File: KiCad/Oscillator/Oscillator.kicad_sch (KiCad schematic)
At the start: 37 parts, among them Q1 NPN, Q2 PNP, Q3 NPN, Q4 PNP, U4 40106, U5 TL074, U7 TL074

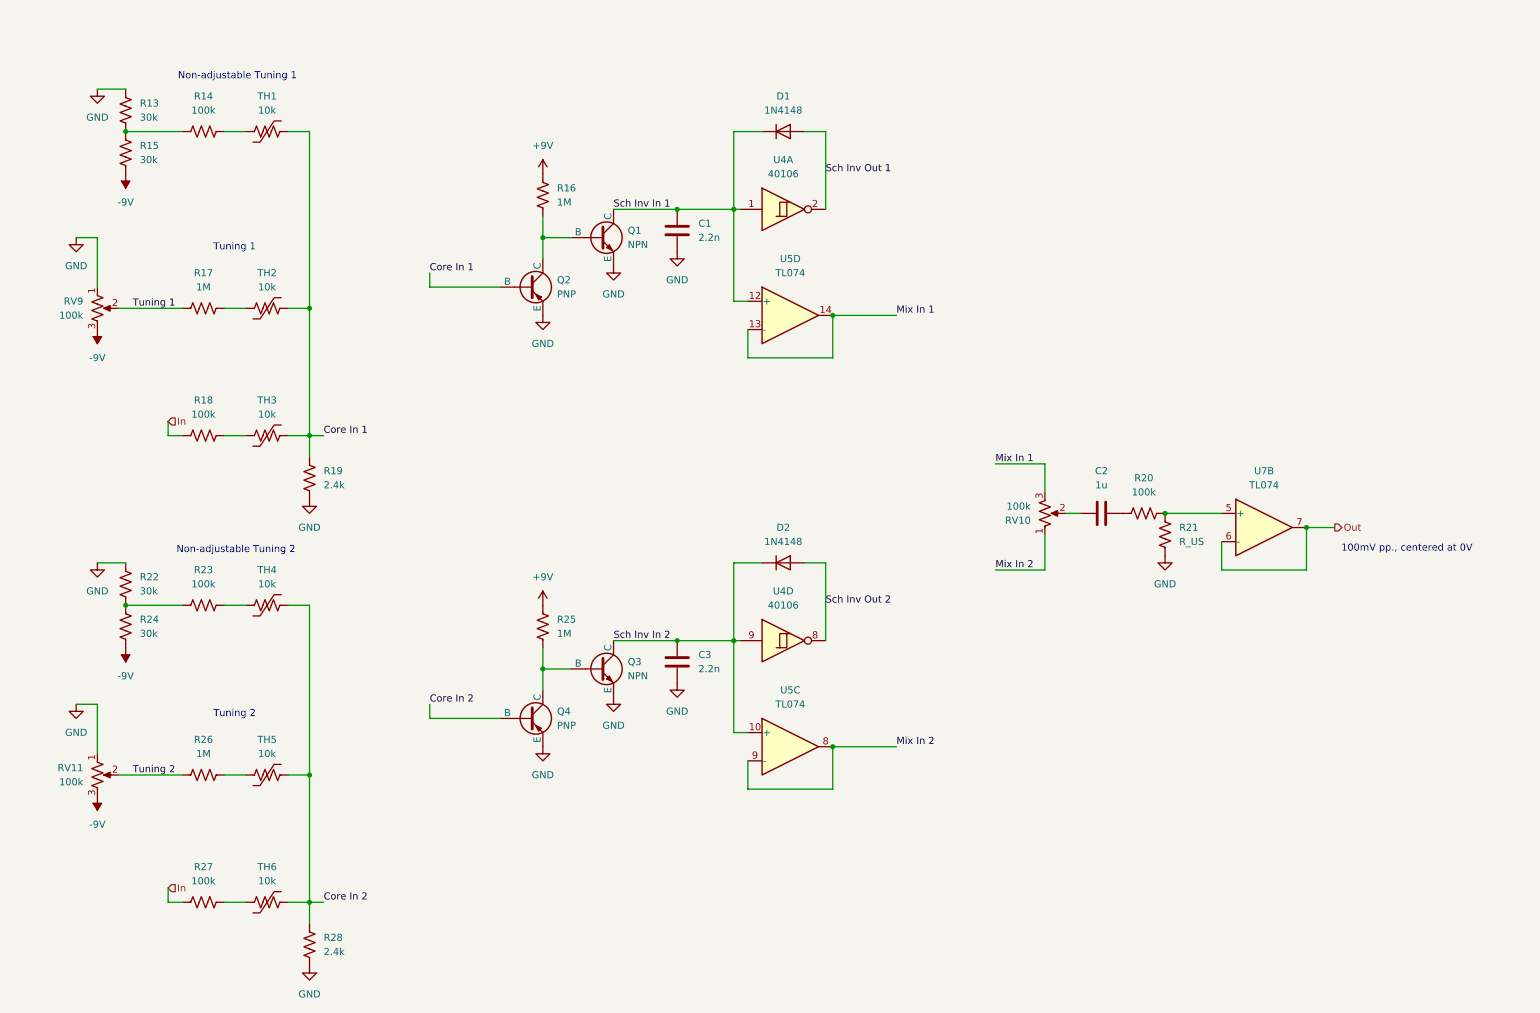
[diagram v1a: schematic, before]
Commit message: finished separating into separate kicad projects
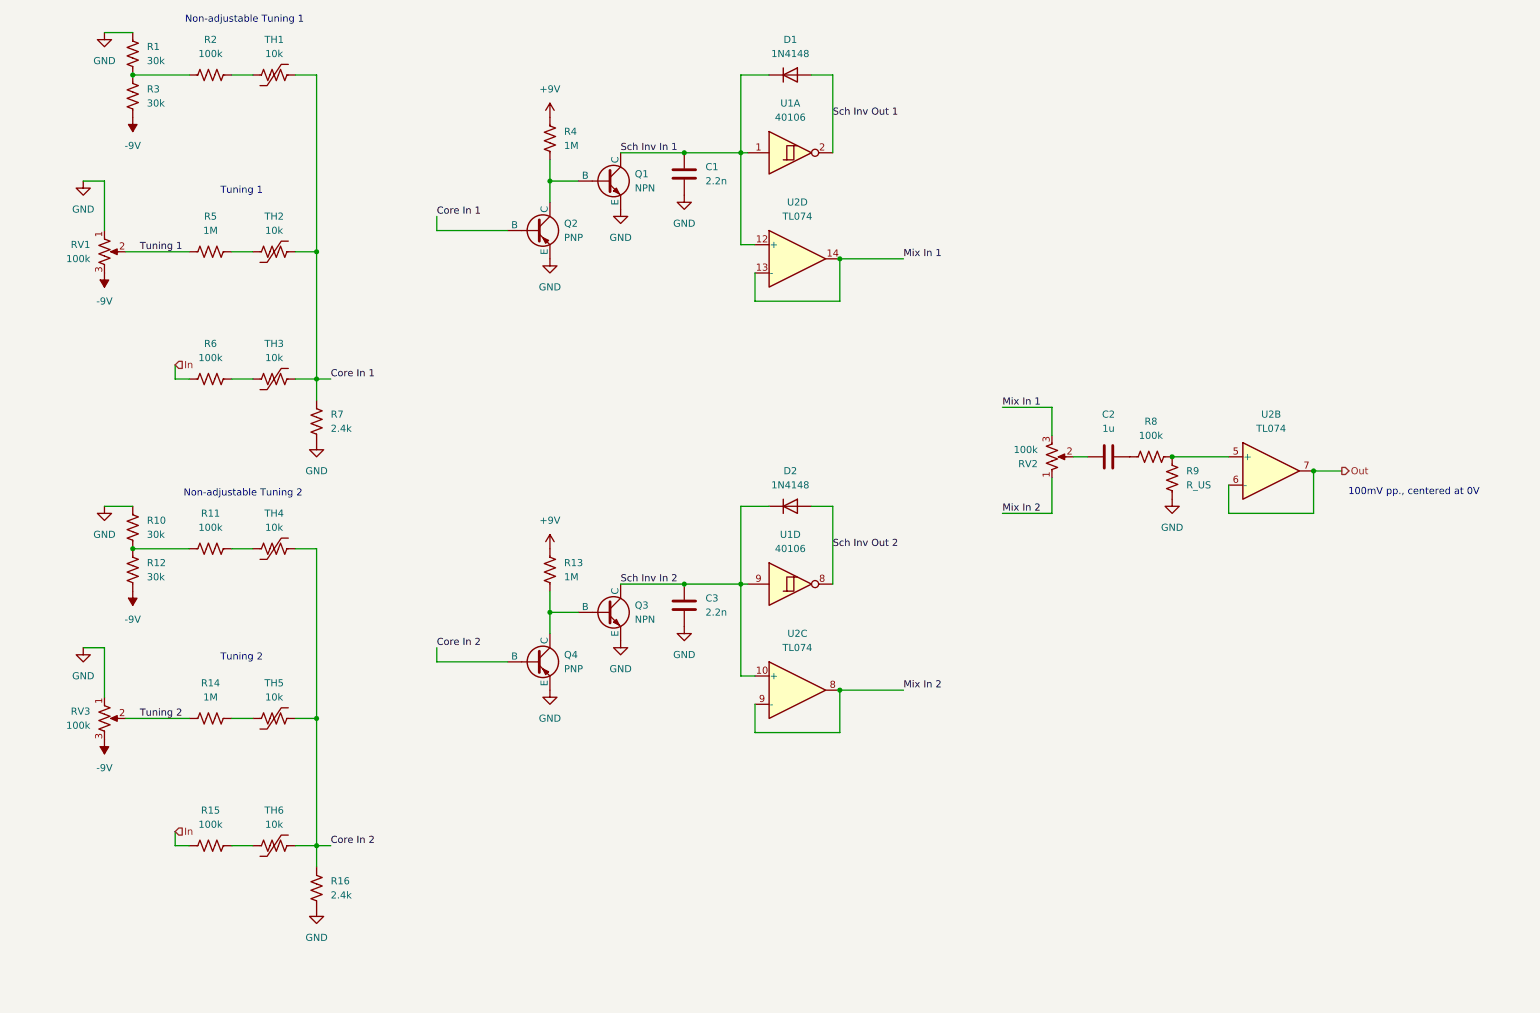
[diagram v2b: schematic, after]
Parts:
- removed RV9: 100k, Potentiometer 100k PTV09A-2020F-B104:Potentiometer 100k PTV09A-2020F-B104, symbol Device:R_Potentiometer_US
- removed U4: 40106, Schmitt Inv. CD40106BE:N14, symbol 4xxx:40106
- removed U5, U7: TL074, Package_DIP:DIP-14_W7.62mm, symbol Amplifier_Operational:TL074
- added RV1: 100k, Potentiometer 100k PTV09A-2020F-B104:Potentiometer 100k PTV09A-2020F-B104, symbol Device:R_Potentiometer_US
- added U1: 40106, Schmitt Inv. CD40106BE:N14, symbol 4xxx:40106
- added U2: TL074, Package_DIP:DIP-14_W7.62mm, symbol Amplifier_Operational:TL074
- renumbered R13 to R1, R22 to R10, R23 to R11, R24 to R12, R25 to R13, R26 to R14, R27 to R15, R28 to R16, R14 to R2, R15 to R3, R16 to R4, R17 to R5, R18 to R6, R19 to R7, R20 to R8, R21 to R9, RV10 to RV2, RV11 to RV3
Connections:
- net -9V: now also RV1.3
- net GND: now also RV1.1
- net Mix In 1: now also U2.13 (-), U2.14
- net Mix In 2: now also U2.8, U2.9 (-)
- net Out: now also U2.6 (-), U2.7
- net Sch Inv In 1: now also U1.1, U2.12 (+)
- net Sch Inv In 2: now also U1.9, U2.10 (+)
- net Sch Inv Out 1: now also U1.2
- net Sch Inv Out 2: now also U1.8
- net Tuning 1: now also RV1.2
- net at R8.2, R9.2: now also U2.5 (+)
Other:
- moved on the sheet: C1, C2, C3, D1, D2, Q1, Q2, Q3, Q4, R1, R10, R11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

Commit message: fixed critical issue in oscillator
schmitt trigger's VEE is supposed to be 0V, not -9V :wilted_rose: :wilted_rose:
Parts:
- removed R8: 100k, Resistor_SMD:R_0603_1608Metric, symbol Device:R_US
- removed R9: R_US, Resistor_THT:R_Axial_DIN0207_L6.3mm_D2.5mm_P7.62mm_Horizontal, symbol Device:R_US
- added J1: Screw_Terminal_01x02, symbol Connector:Screw_Terminal_01x02
- added RV3: 100k, symbol Device:R_Potentiometer_Trim_US
- added U3: TL074, Package_DIP:DIP-14_W7.62mm, symbol Amplifier_Operational:TL074
- renumbered R12 to R10, R13 to R11, R14 to R12, R15 to R13, R16 to R14, R10 to R8, R11 to R9, RV3 to RV4
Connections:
- net GND: now also RV3.3
- net In: now also J1.1 (Pin_1)
- net Out: now also J1.2 (Pin_2)
- net at U2.5 (+): now also RV3.2
- net at C2.2: now also RV3.1
- net at C2.1: now also U3.6 (-), U3.7; no longer RV2.2
- new net: RV2.2, U3.5 (+)
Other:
- moved on the sheet: C2, RV2, U2B

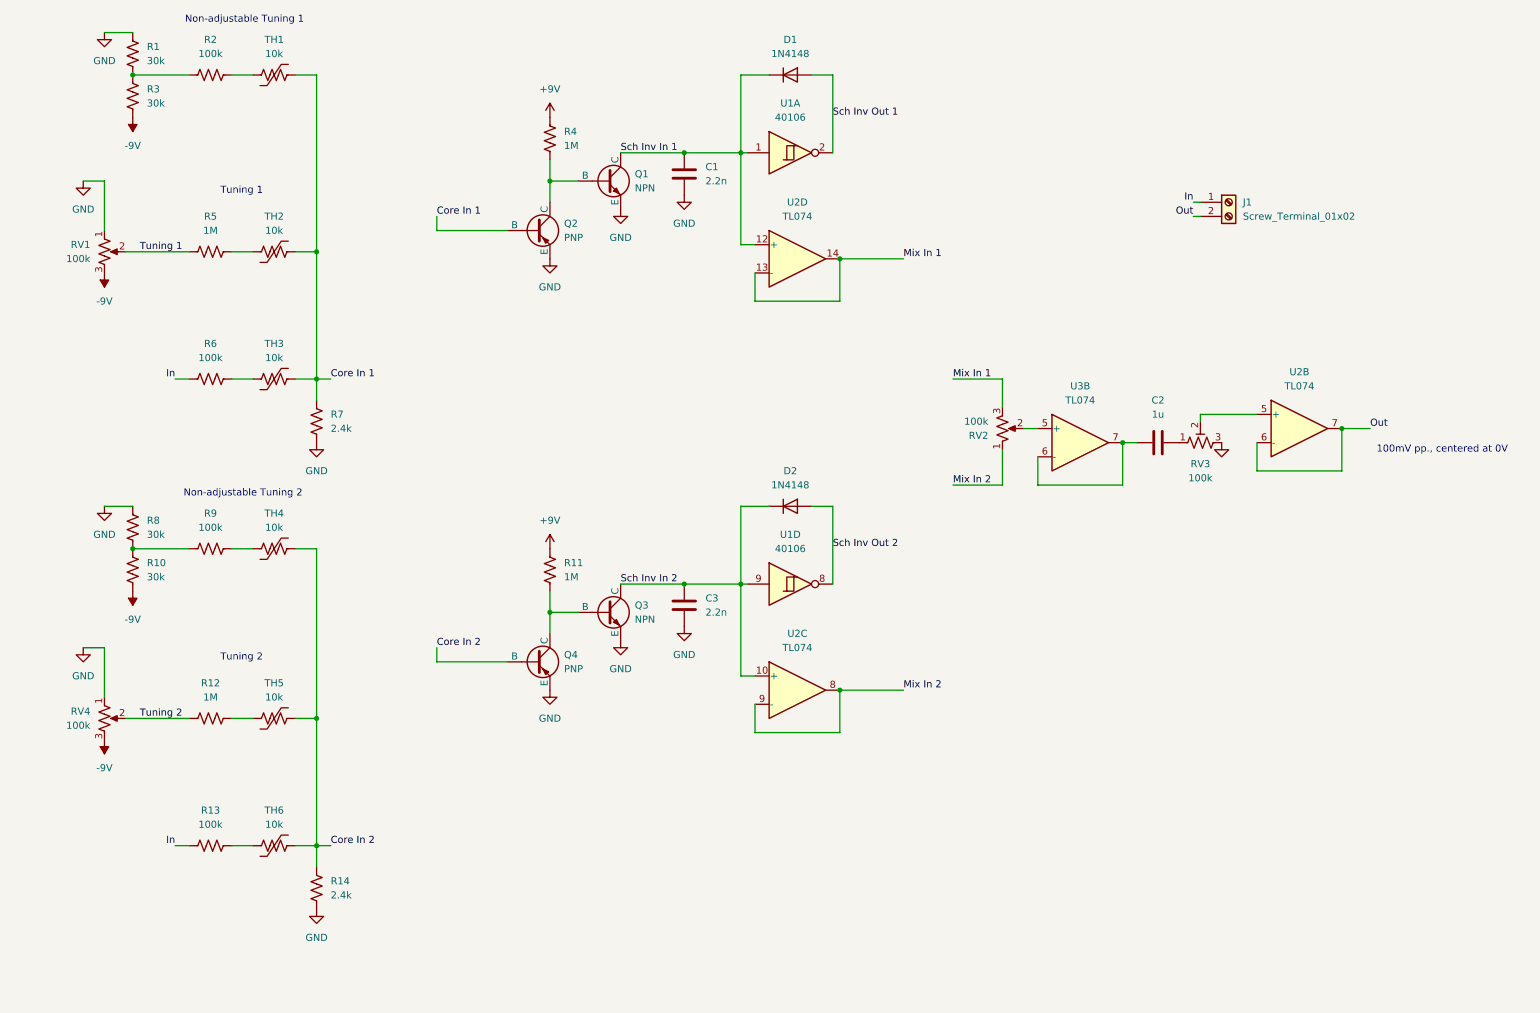
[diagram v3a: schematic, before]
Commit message: made oscillator more adjustable
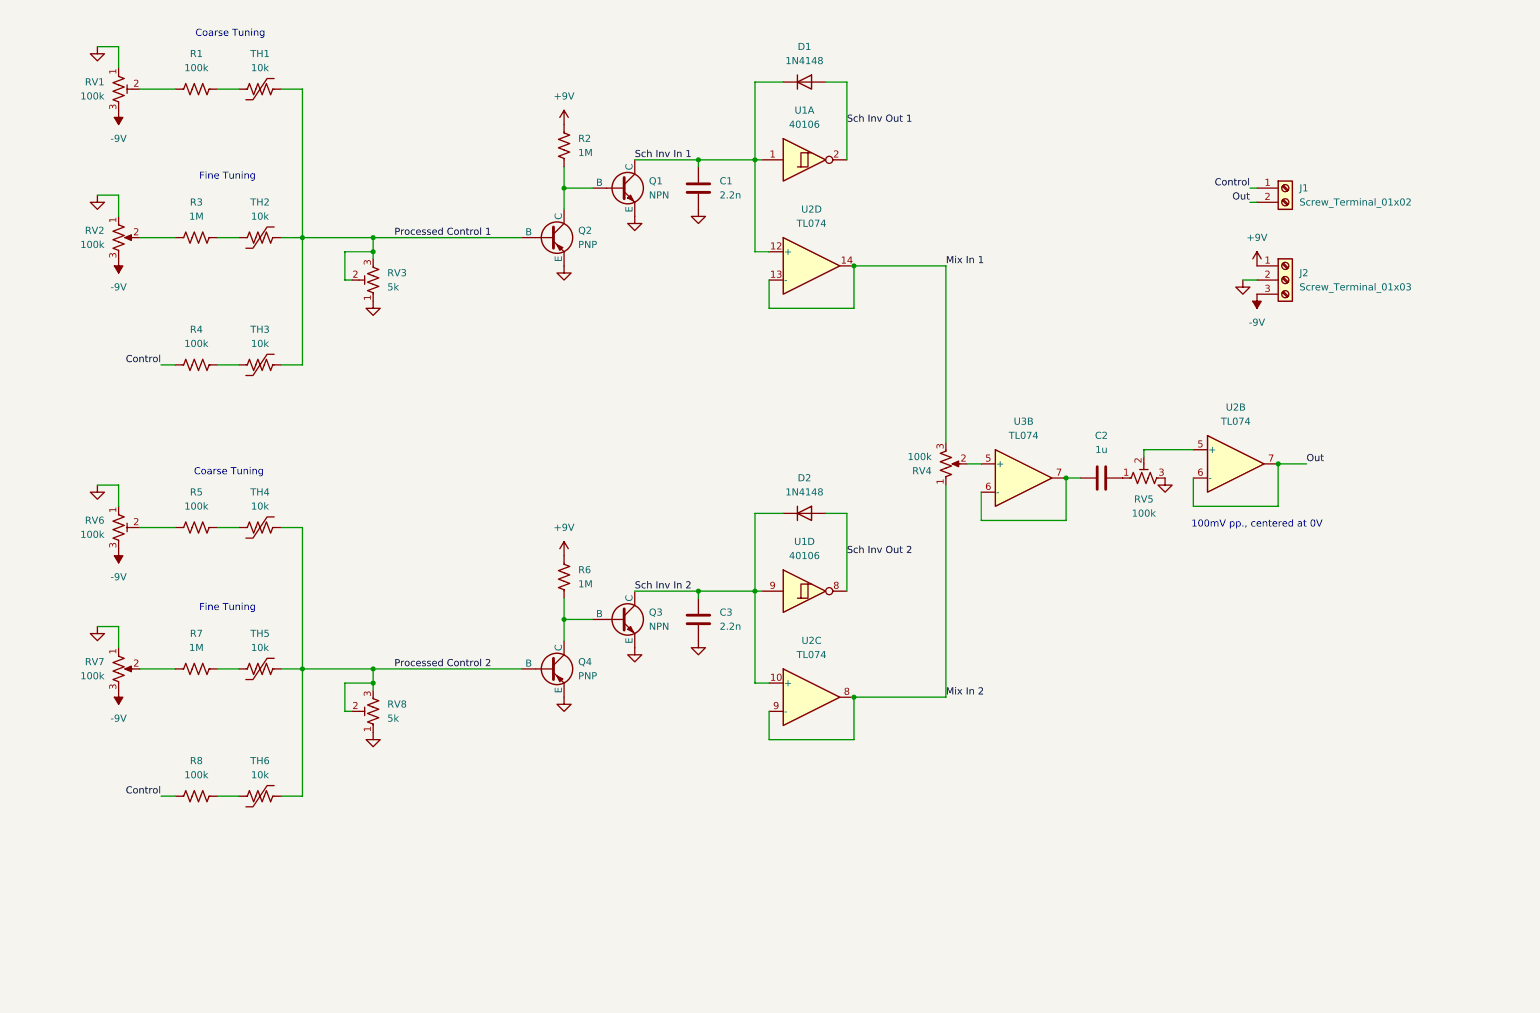
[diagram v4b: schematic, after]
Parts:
- removed R1, R10, R3, R8: 30k, Resistor_SMD:R_0603_1608Metric, symbol Device:R_US
- removed R14, R7: 2.4k, Resistor_SMD:R_0603_1608Metric, symbol Device:R_US
- added J2: Screw_Terminal_01x03, symbol Connector:Screw_Terminal_01x03
- added RV1, RV6: 100k, symbol Device:R_Potentiometer_Trim_US
- added RV3, RV8: 5k, symbol Device:R_Potentiometer_Trim_US
- renumbered R2 to R1, R4 to R2, R5 to R3, R6 to R4, R9 to R5, R11 to R6, R12 to R7, R13 to R8, RV1 to RV2, RV2 to RV4, RV3 to RV5, RV4 to RV7
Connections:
- net +9V: now also J2.1 (Pin_1)
- net -9V: now also J2.3 (Pin_3), RV1.3, RV6.3
- net GND: now also J2.2 (Pin_2), RV1.1, RV3.1, RV6.1, RV8.1
- net at R1.1: now also RV1.2
- net at R5.1: now also RV6.2
- net Core In 1 renamed Processed Control 1
- net Processed Control 1: now also RV3.2, RV3.3
- net Core In 2 renamed Processed Control 2
- net Processed Control 2: now also RV8.2, RV8.3
- net In renamed Control
- net Tuning 1: no longer names the net of R3.1, RV2.2
- net Tuning 2: no longer names the net of R7.1, RV7.2
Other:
- note added: "Coarse Tuning"
- note added: "Fine Tuning"
- note removed: "Non-adjustable Tuning 1"
- note removed: "Non-adjustable Tuning 2"
- note removed: "Tuning 1"
- note removed: "Tuning 2"
- moved on the sheet: C1, C2, C3, D1, D2, J1, Q1, Q2, Q3, Q4, R1, R2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

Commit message: added test points
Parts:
- added TP? (x21): TestPoint_Small, symbol Connector:TestPoint_Small
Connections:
- net -9V: now also TP?.1, TP?.1, TP?.1, TP?.1
- net Control: now also TP?.1
- net GND: now also TP?.1, TP?.1, TP?.1, TP?.1, TP?.1, TP?.1
- net Mix In 1: now also TP?.1
- net Mix In 2: now also TP?.1
- net Out: now also TP?.1
- net Processed Control 1: now also TP?.1
- net Processed Control 2: now also TP?.1
- net at R3.1, RV2.2: now also TP?.1
- net at R1.1, RV1.2: now also TP?.1
- net at R7.1, RV7.2: now also TP?.1
- net at R5.1, RV6.2: now also TP?.1
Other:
- moved on the sheet: R1, RV1, RV2, RV6, RV7, TH1
